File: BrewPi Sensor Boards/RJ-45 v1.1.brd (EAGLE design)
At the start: 31.4 x 39.4 mm, 9 parts, among them J1 RJ45-8X

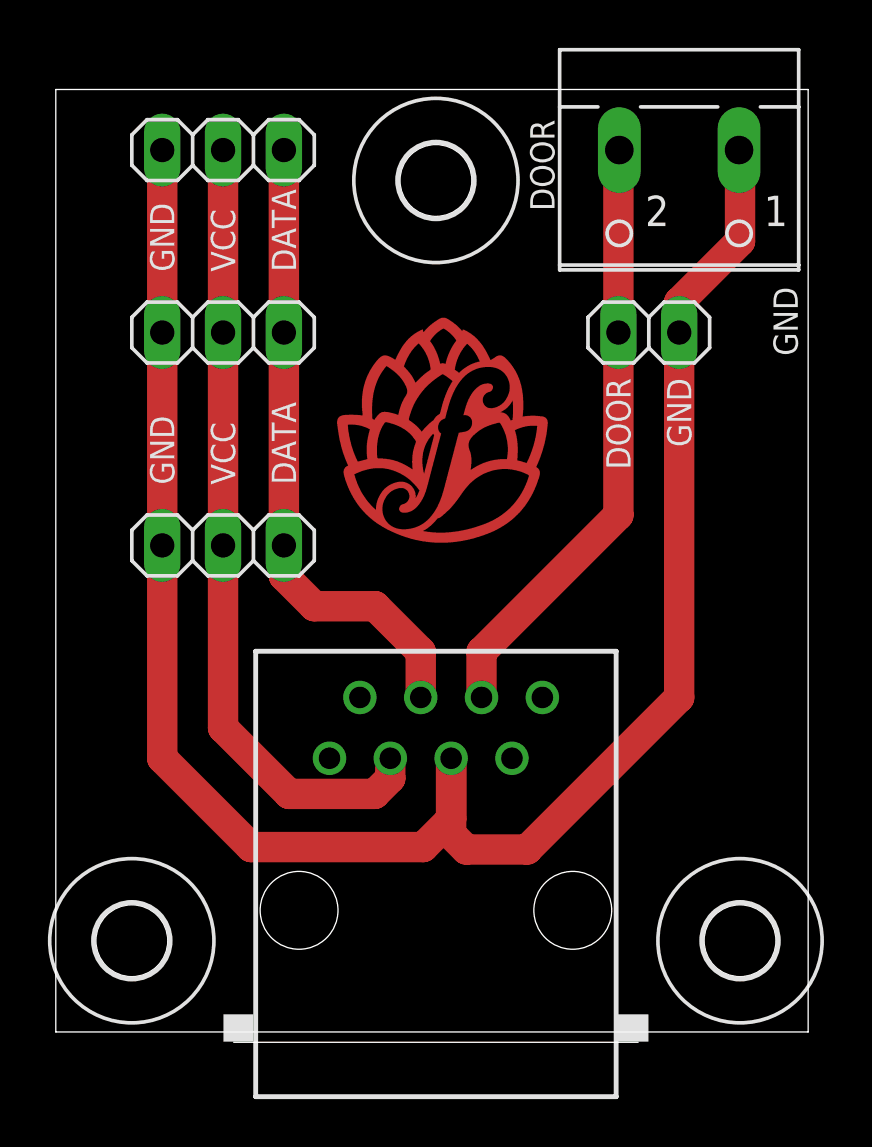
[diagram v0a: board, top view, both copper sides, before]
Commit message: Finalize main PCB BOM
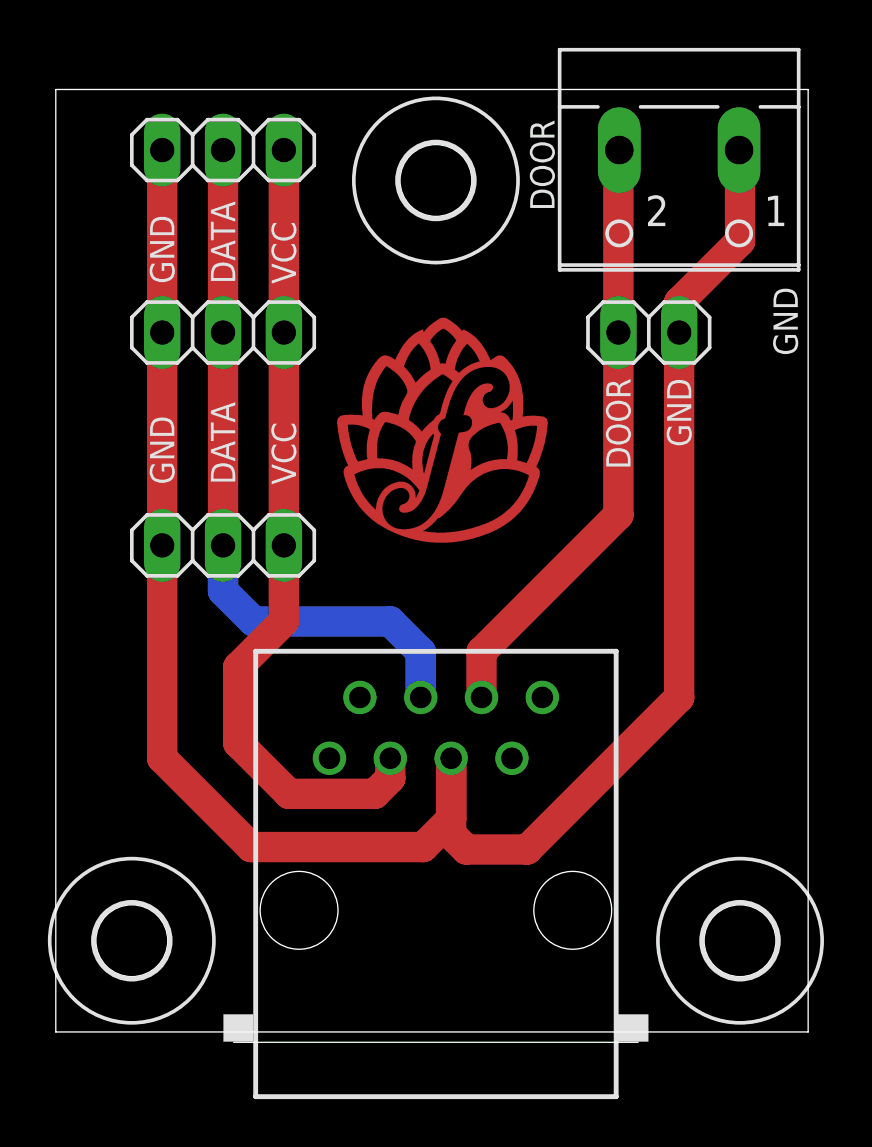
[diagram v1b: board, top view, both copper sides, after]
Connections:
- net ONEWIRE: now also JP1.2, JP2.2, JP3.2; no longer JP1.3, JP2.3, JP3.3
- net VCC: now also JP1.3, JP2.3, JP3.3; no longer JP1.2, JP2.2, JP3.2
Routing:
- net ONEWIRE: track 26.7 -> 29.6 mm
- net VCC: track 33.4 -> 33.9 mm
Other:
- board text added: "RJ-45 Breakout Board v1.1 @thorrak says hi"
- board text removed: "RJ-45 Breakout Board v1.1 Top Routed @thorrak says hi"
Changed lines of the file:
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@@
 <setting verticaltext="up"/>
 </settings>
-<grid distance="0.05" unitdist="inch" unit="inch" style="lines" multiple="1" display="yes" altdistance="0.025" altunitdist="inch" altunit="inch"/>
+<grid distance="0.025" unitdist="inch" unit="inch" style="lines" multiple="2" display="yes" altdistance="0.0125" altunitdist="inch" altunit="inch"/>
 <layers>
-<layer number="1" name="Top" color="4" fill="1" visible="no" active="yes"/>
+<layer number="1" name="Top" color="4" fill="1" visible="yes" active="yes"/>
 <layer number="16" name="Bottom" color="1" fill="1" visible="yes" active="yes"/>
 <layer number="17" name="Pads" color="2" fill="1" visible="yes" active="yes"/>
@@
 <text x="24.765" y="31.115" size="1.016" layer="25" font="vector" ratio="12" rot="R90" align="center-right">GND</text>
 <text x="3.175" y="26.67" size="1.016" layer="25" font="vector" ratio="12" rot="R90" align="center-left">GND</text>
-<text x="5.715" y="26.67" size="1.016" layer="25" font="vector" ratio="12" rot="R90" align="center-left">VCC</text>
+<text x="8.255" y="26.67" size="1.016" layer="25" font="vector" ratio="12" rot="R90" align="center-left">VCC</text>
 <text x="22.225" y="31.115" size="1.016" layer="25" font="vector" ratio="12" rot="R90" align="center-right">DOOR</text>
-<text x="8.255" y="26.67" size="1.016" layer="25" font="vector" ratio="12" rot="R90" align="center-left">DATA</text>
+<text x="5.715" y="26.67" size="1.016" layer="25" font="vector" ratio="12" rot="R90" align="center-left">DATA</text>
 <text x="29.21" y="16.51" size="1.016" layer="26" font="vector" ratio="12" rot="MR0">RJ-45 Pinout:
 3 - VCC (3v3 or 5v)
@@
 5 - GND
 6 - Door</text>
-<text x="8.255" y="35.56" size="1.016" layer="25" font="vector" ratio="12" rot="R90" align="center-left">DATA</text>
-<text x="5.715" y="35.56" size="1.016" layer="25" font="vector" ratio="12" rot="R90" align="center-left">VCC</text>
-<text x="3.175" y="35.56" size="1.016" layer="26" font="vector" ratio="12" rot="MR90" align="center-left">GND</text>
+<text x="5.715" y="35.052" size="1.016" layer="25" font="vector" ratio="12" rot="R90" align="center-left">DATA</text>
+<text x="8.255" y="35.052" size="1.016" layer="25" font="vector" ratio="12" rot="R90" align="center-left">VCC</text>
+<text x="3.175" y="35.052" size="1.016" layer="26" font="vector" ratio="12" rot="MR90" align="center-left">GND</text>
 <text x="29.21" y="26.67" size="1.016" layer="26" font="vector" ratio="12" rot="MR0">RJ-45 Breakout Board
-v1.1 Top Routed
+v1.1
 @thorrak says hi</text>
 <text x="29.21" y="34.925" size="1.016" layer="25" font="vector" ratio="12" rot="R90" align="center-right">GND</text>
@@
 <rectangle x1="14.84350625" y1="33.6288375" x2="14.9893" y2="33.63239375" layer="1"/>
 <rectangle x1="14.84350625" y1="33.63239375" x2="14.9893" y2="33.63595" layer="1"/>
-<text x="3.175" y="35.56" size="1.016" layer="25" font="vector" ratio="12" rot="R90" align="center-left">GND</text>
-<text x="5.715" y="35.56" size="1.016" layer="26" font="vector" ratio="12" rot="MR90" align="center-left">VCC</text>
-<text x="5.715" y="26.67" size="1.016" layer="26" font="vector" ratio="12" rot="MR90" align="center-left">VCC</text>
+<text x="3.175" y="35.052" size="1.016" layer="25" font="vector" ratio="12" rot="R90" align="center-left">GND</text>
+<text x="8.255" y="35.052" size="1.016" layer="26" font="vector" ratio="12" rot="MR90" align="center-left">VCC</text>
+<text x="8.255" y="26.67" size="1.016" layer="26" font="vector" ratio="12" rot="MR90" align="center-left">VCC</text>
 <text x="3.175" y="26.67" size="1.016" layer="26" font="vector" ratio="12" rot="MR90" align="center-left">GND</text>
-<text x="8.255" y="35.56" size="1.016" layer="26" font="vector" ratio="12" rot="MR90" align="center-left">DATA</text>
-<text x="8.255" y="26.67" size="1.016" layer="26" font="vector" ratio="12" rot="MR90" align="center-left">DATA</text>
+<text x="5.715" y="35.052" size="1.016" layer="26" font="vector" ratio="12" rot="MR90" align="center-left">DATA</text>
+<text x="5.715" y="26.67" size="1.016" layer="26" font="vector" ratio="12" rot="MR90" align="center-left">DATA</text>
 <text x="22.225" y="38.481" size="1.016" layer="26" font="vector" ratio="12" rot="MR90" align="center-right">DOOR</text>
 <text x="27.305" y="38.481" size="1.016" layer="26" font="vector" ratio="12" rot="MR90" align="center-right">GND</text>
@@
 <signals>
 <signal name="ONEWIRE">
-<contactref element="JP2" pad="3"/>
-<contactref element="JP1" pad="3"/>
-<contactref element="JP3" pad="3"/>
 <contactref element="J1" pad="4"/>
-<wire x1="8.255" y1="40.64" x2="8.255" y2="33.02" width="1.27" layer="1"/>
-<wire x1="8.255" y1="33.02" x2="8.255" y2="24.13" width="1.27" layer="1"/>
-<wire x1="13.97" y1="17.78" x2="13.97" y2="19.685" width="1.27" layer="1"/>
-<wire x1="9.525" y1="21.59" x2="8.255" y2="22.86" width="1.27" layer="1"/>
-<wire x1="8.255" y1="22.86" x2="8.255" y2="24.13" width="1.27" layer="1"/>
-<wire x1="13.97" y1="19.685" x2="12.065" y2="21.59" width="1.27" layer="1"/>
-<wire x1="12.065" y1="21.59" x2="9.525" y2="21.59" width="1.27" layer="1"/>
-</signal>
-<signal name="VCC">
-<contactref element="JP2" pad="2"/>
 <contactref element="JP1" pad="2"/>
+<contactref element="JP2" pad="2"/>
 <contactref element="JP3" pad="2"/>
+<wire x1="13.97" y1="17.78" x2="13.97" y2="19.685" width="1.27" layer="16"/>
+<wire x1="13.97" y1="19.685" x2="12.7" y2="20.955" width="1.27" layer="16"/>
+<wire x1="6.985" y1="20.955" x2="12.7" y2="20.955" width="1.27" layer="16"/>
+<wire x1="5.715" y1="24.13" x2="5.715" y2="22.225" width="1.27" layer="16"/>
+<wire x1="5.715" y1="22.225" x2="6.985" y2="20.955" width="1.27" layer="16"/>
+<wire x1="5.715" y1="24.13" x2="5.715" y2="33.02" width="1.27" layer="1"/>
+<wire x1="5.715" y1="33.02" x2="5.715" y2="40.64" width="1.27" layer="1"/>
+</signal>
+<signal name="VCC">
 <contactref element="J1" pad="3"/>
-<wire x1="5.715" y1="16.51" x2="5.715" y2="24.13" width="1.27" layer="1"/>
 <wire x1="12.7" y1="15.24" x2="12.7" y2="14.40649375" width="1.27" layer="1"/>
 <wire x1="12.7" y1="14.40649375" x2="12.04610625" y2="13.7526" width="1.27" layer="1"/>
 <wire x1="12.04610625" y1="13.7526" x2="8.4724" y2="13.7526" width="1.27" layer="1"/>
-<wire x1="8.4724" y1="13.7526" x2="5.715" y2="16.51" width="1.27" layer="1"/>
-<wire x1="5.715" y1="24.13" x2="5.715" y2="33.02" width="1.27" layer="1"/>
-<wire x1="5.715" y1="33.02" x2="5.715" y2="40.64" width="1.27" layer="1"/>
+<wire x1="8.4724" y1="13.7526" x2="6.35" y2="15.875" width="1.27" layer="1"/>
+<contactref element="JP3" pad="3"/>
+<contactref element="JP2" pad="3"/>
+<contactref element="JP1" pad="3"/>
+<wire x1="8.255" y1="40.64" x2="8.255" y2="33.02" width="1.27" layer="1"/>
+<wire x1="8.255" y1="33.02" x2="8.255" y2="24.13" width="1.27" layer="1"/>
+<wire x1="8.255" y1="24.13" x2="8.255" y2="20.955" width="1.27" layer="1"/>
+<wire x1="8.255" y1="20.955" x2="6.35" y2="19.05" width="1.27" layer="1"/>
+<wire x1="6.35" y1="19.05" x2="6.35" y2="15.875" width="1.27" layer="1"/>
 </signal>
 <signal name="GND">

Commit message: Update sensor breakout board
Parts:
- J1: device con-tycoelectronics:RJ45-NO-SHIELD -> Donnie:RJ45-NS-XDIM
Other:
- outline, holes or cut-outs redrawn
